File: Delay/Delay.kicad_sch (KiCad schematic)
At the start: 40 parts, among them J101 Conn_02x08_Odd_Even, J102 AudioJack2_SwitchT, U101 TL072, U102 TL072, U103 TL072, U104 TL072, U105 TL072, U106 TL072, U107 TL072, U108 TL072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

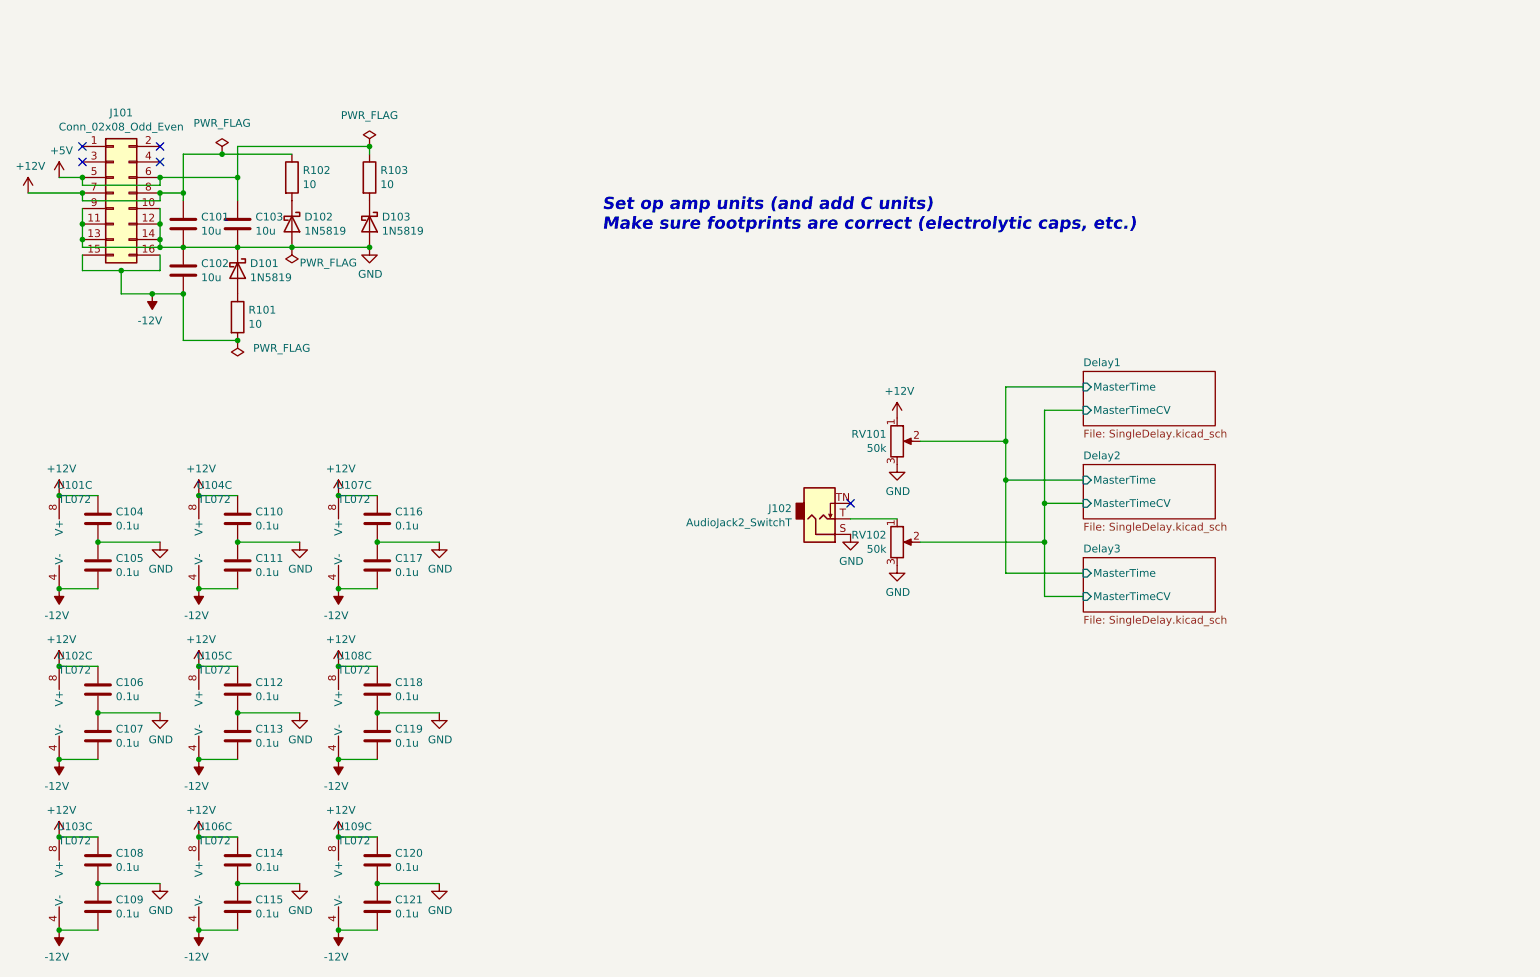
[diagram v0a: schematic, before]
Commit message: Add delay daisy chaining switches and readme
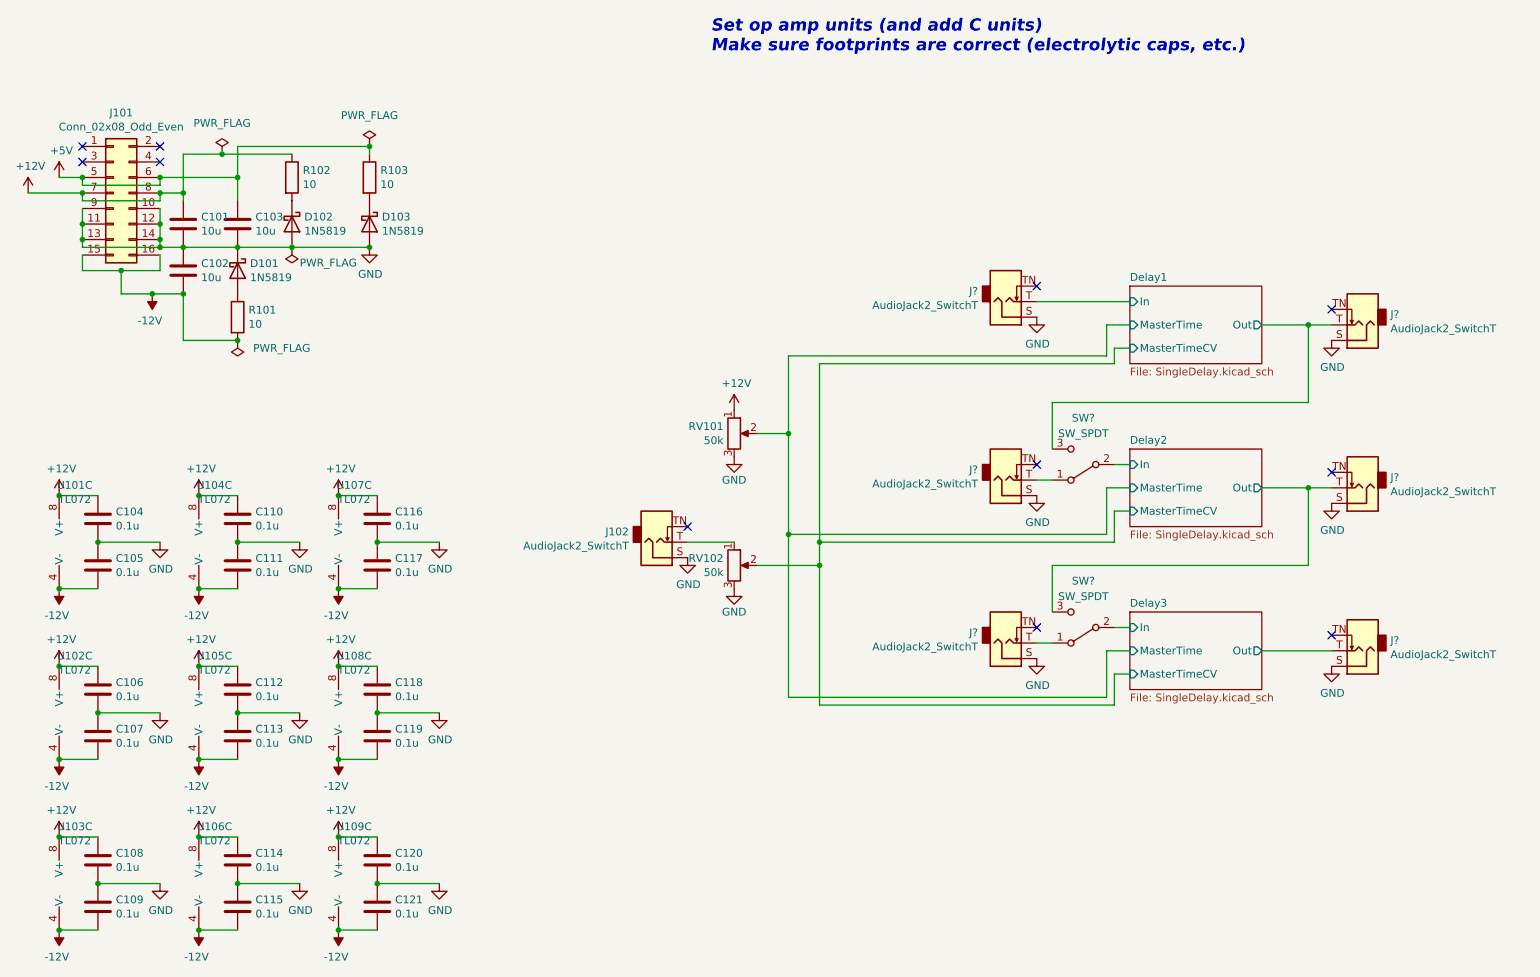
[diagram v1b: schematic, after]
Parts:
- added J? (x6): AudioJack2_SwitchT, symbol Connector:AudioJack2_SwitchT
- added SW? (x2): SW_SPDT, symbol Switch:SW_SPDT
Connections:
- net GND: now also J?.S, J?.S, J?.S, J?.S, J?.S, J?.S
- new net: J?.T, SW?.1 (A) (x2)
- new net Delay1/In: J?.T
- new net Delay1/Out: J?.T, SW?.3 (C)
- new net Delay2/In: SW?.2 (B)
- new net Delay2/Out: J?.T, SW?.3 (C)
- new net Delay3/In: SW?.2 (B)
- new net Delay3/Out: J?.T
- no-connect marks 5 -> 11
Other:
- sheet Delay1 ports: added In, Out; removed none
- sheet Delay2 ports: added In, Out; removed none
- sheet Delay3 ports: added In, Out; removed none
- moved on the sheet: J102, RV101, RV102

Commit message: Finish delay PCB
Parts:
- removed C104, C105, C106, C107, C108, C109, C110, C111, C112, C113, C114, C115, C116, C117, C118, C119, C120, C121: 0.1u, symbol Device:C
- removed U101, U102, U103, U104, U105, U106, U107, U108, U109: TL072, symbol Amplifier_Operational:TL072
- J102: footprint (none) -> Connector_Audio:Jack_3.5mm_QingPu_WQP-PJ398SM_Vertical_CircularHoles
- J103, J104, J105, J106, J107, J108: renamed from J?; footprint (none) -> Connector_Audio:Jack_3.5mm_QingPu_WQP-PJ398SM_Vertical_CircularHoles
- RV101, RV102: footprint (none) -> Potentiometer_THT:Potentiometer_Alpha_RD901F-40-00D_Single_Vertical_CircularHoles
- SW101, SW102: renamed from SW?; footprint (none) -> Custom:MTS-102_MTS-103_MTS-112_MTS-113_MTS-123
- renumbered C101 to C107, C102 to C108, C103 to C109
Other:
- note removed: "Set op amp units (and add C units) Make sure footprints are correct (electrolytic caps, etc.)"
- moved on the sheet: C107, C108, C109, D101, D102, D103, J101, R101, R102, R103
